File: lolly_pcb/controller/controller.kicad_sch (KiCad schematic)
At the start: 1 part, among them U1 ESP32-S2-MINI-1

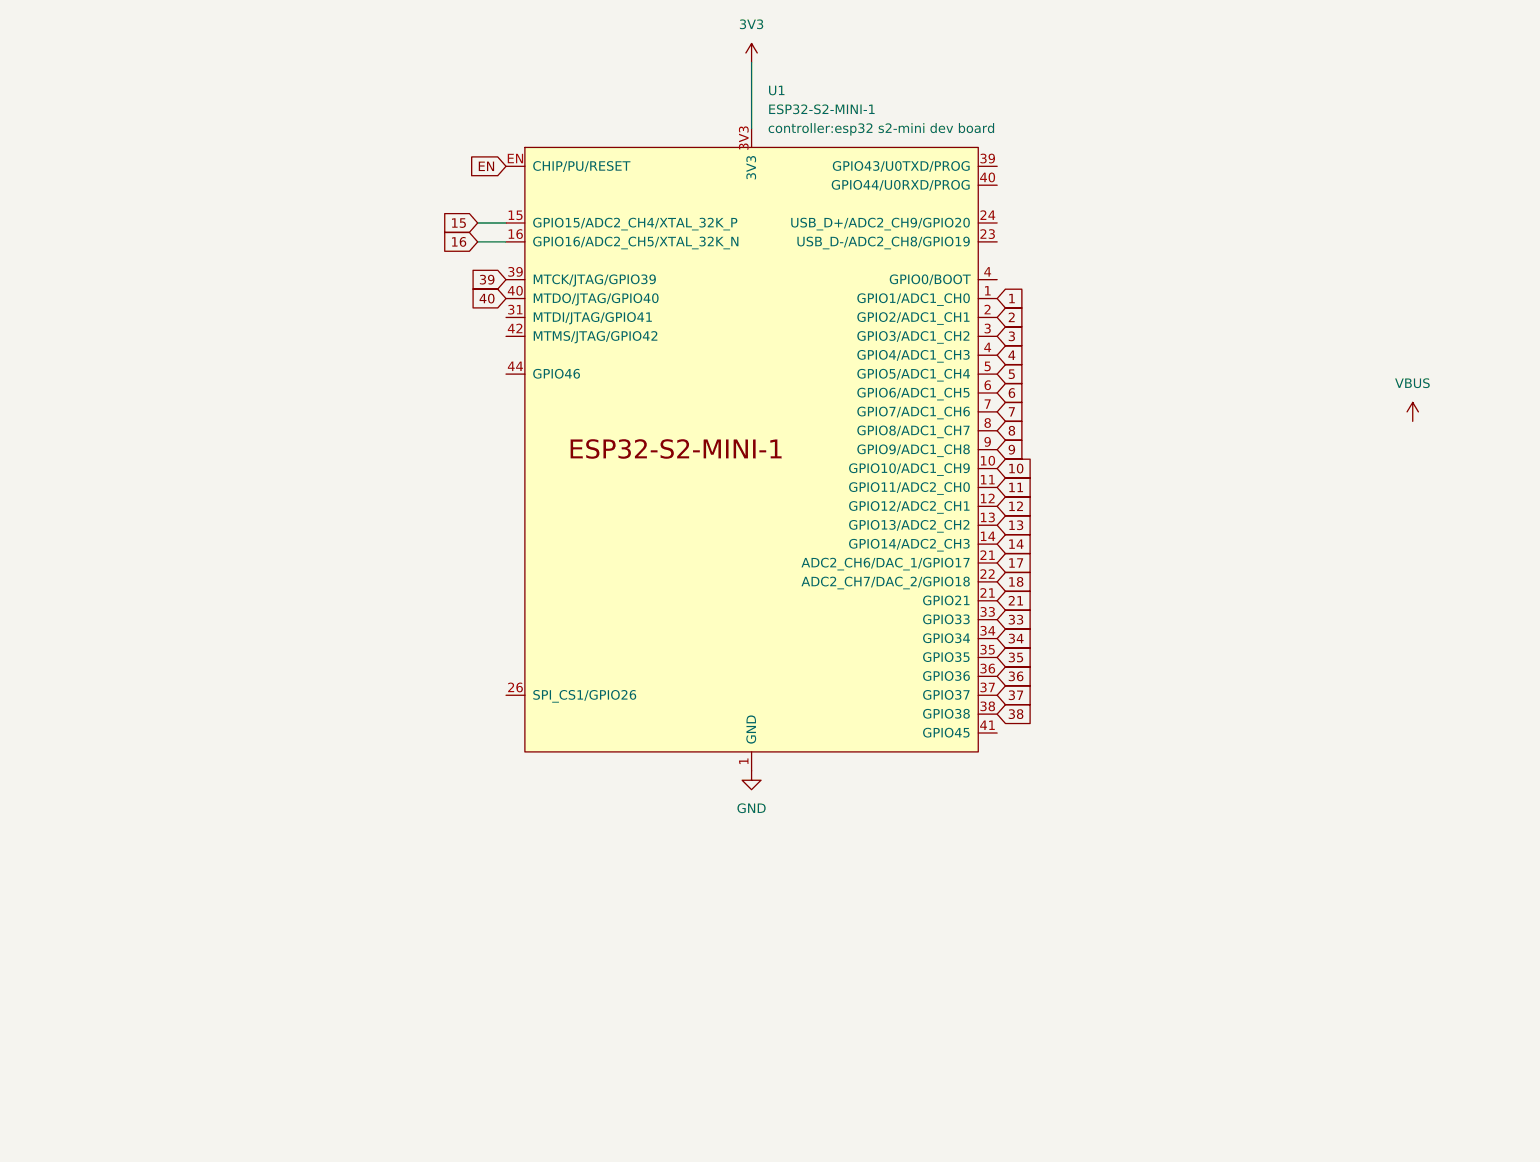
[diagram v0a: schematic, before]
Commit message: add charging circuit, connector and switch
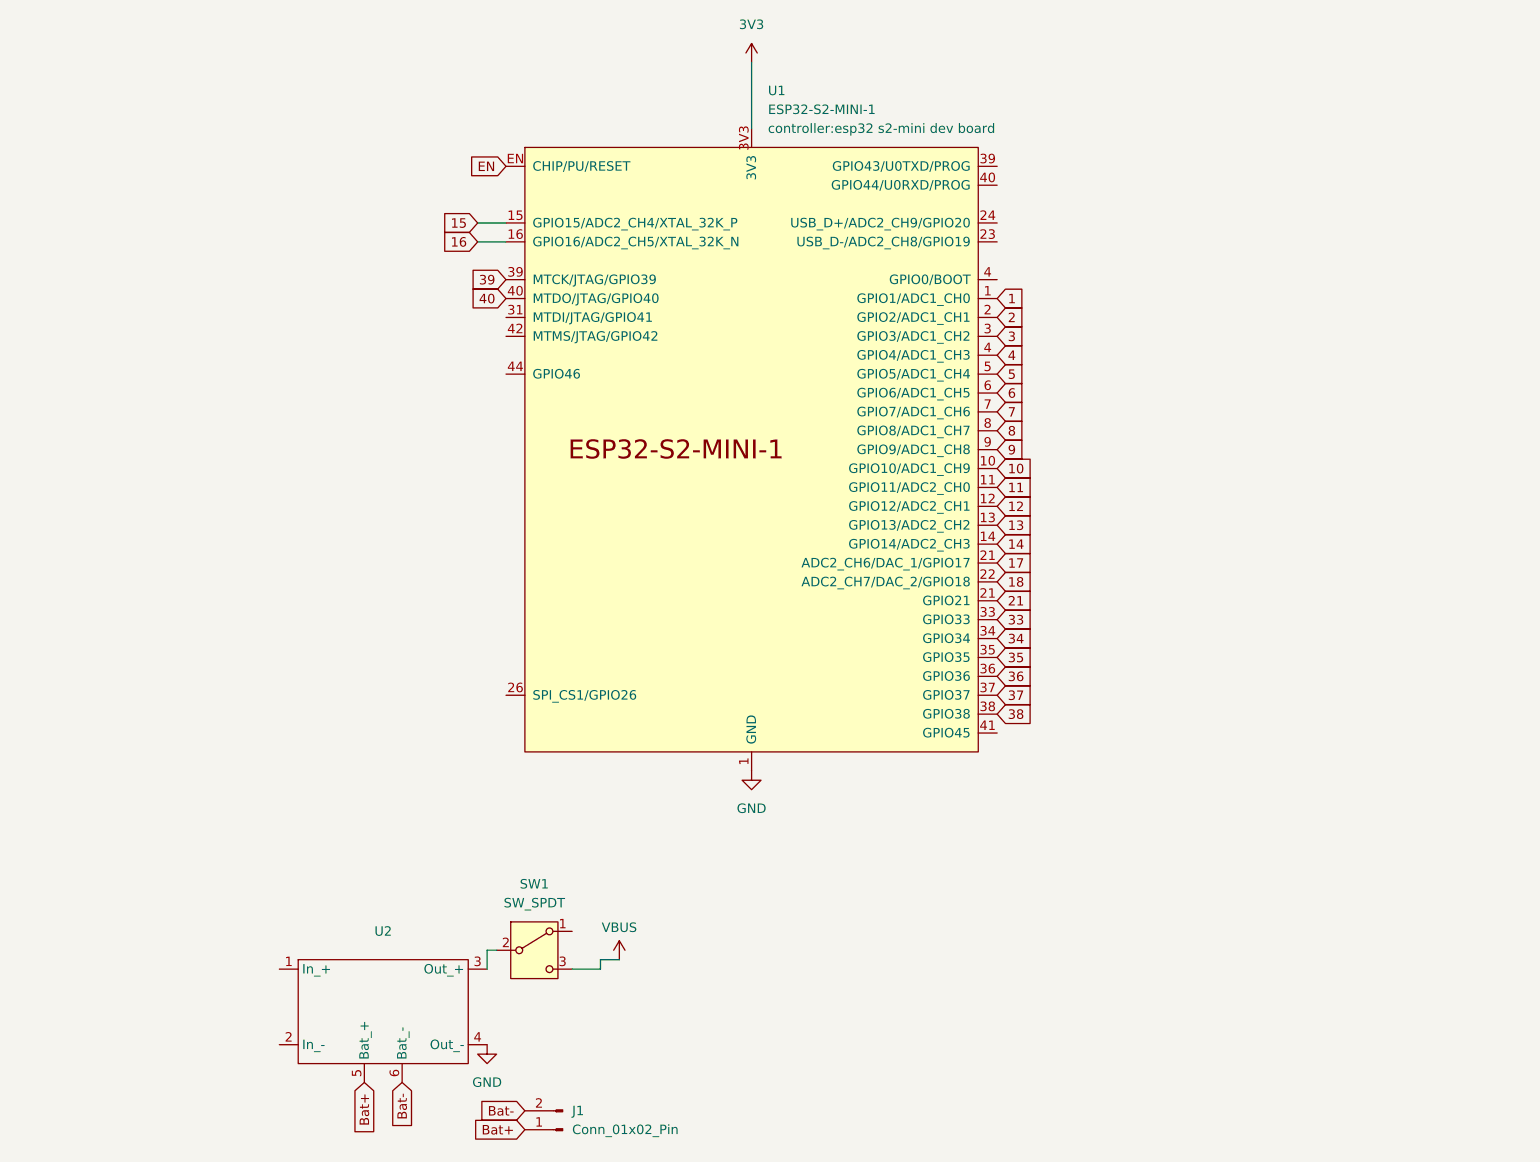
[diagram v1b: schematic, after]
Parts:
- added J1: Conn_01x02_Pin, Connector_JST:JST_PH_S2B-PH-K_1x02_P2.00mm_Horizontal, symbol Connector:Conn_01x02_Pin
- added SW1: SW_SPDT, controller:1P2T SPDT RUNCCI-YUN, symbol Switch:SW_SPDT
- added U2: ~, controller:tp4056 module, symbol lolly_comp:tp4056_module
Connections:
- net GND: now also U2.4 (Out_-)
- net VBUS: now also SW1.3 (C)
- new net: SW1.2 (B), U2.3 (Out_+)
- new net Bat+: J1.1 (Pin_1), U2.5 (Bat_+)
- new net Bat-: J1.2 (Pin_2), U2.6 (Bat_-)

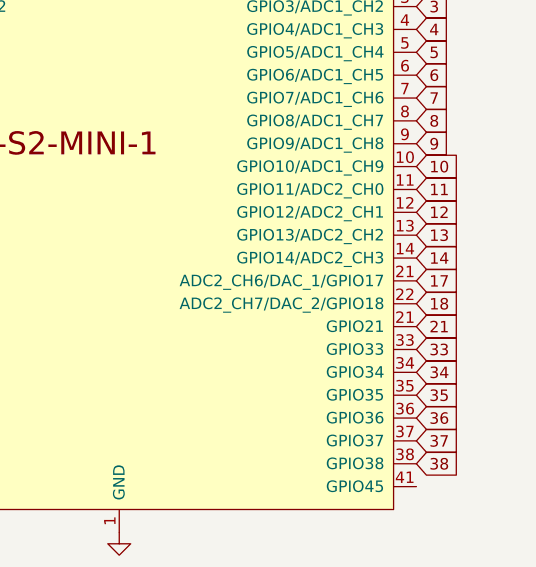
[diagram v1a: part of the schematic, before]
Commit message: first proper layout
includes solder pads for later components, better antenna placement, and routing
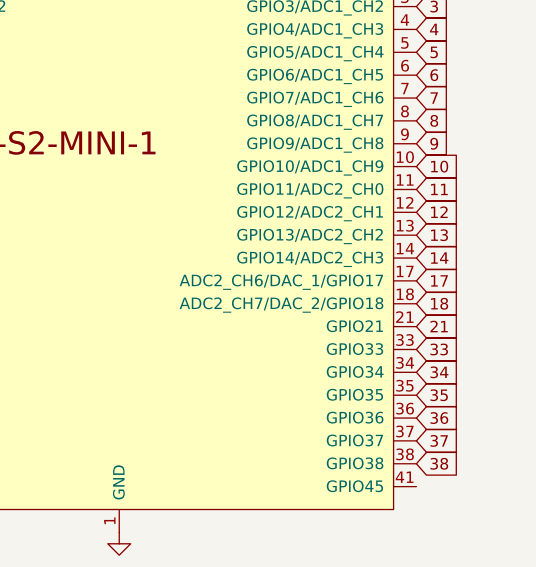
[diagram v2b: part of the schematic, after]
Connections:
- net 17: now also U1.17 (ADC2_CH6/DAC_1/GPIO17); no longer U1.21 (GPIO21)
- net 18: now also U1.18 (ADC2_CH7/DAC_2/GPIO18); no longer U1.22 (ADC2_CH7/DAC_2/GPIO18)
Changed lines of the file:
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@@
 		(pin "21"
 		)
-		(pin "21"
+		(pin "17"
 		)
-		(pin "22"
+		(pin "18"
 		)
 		(pin "23"

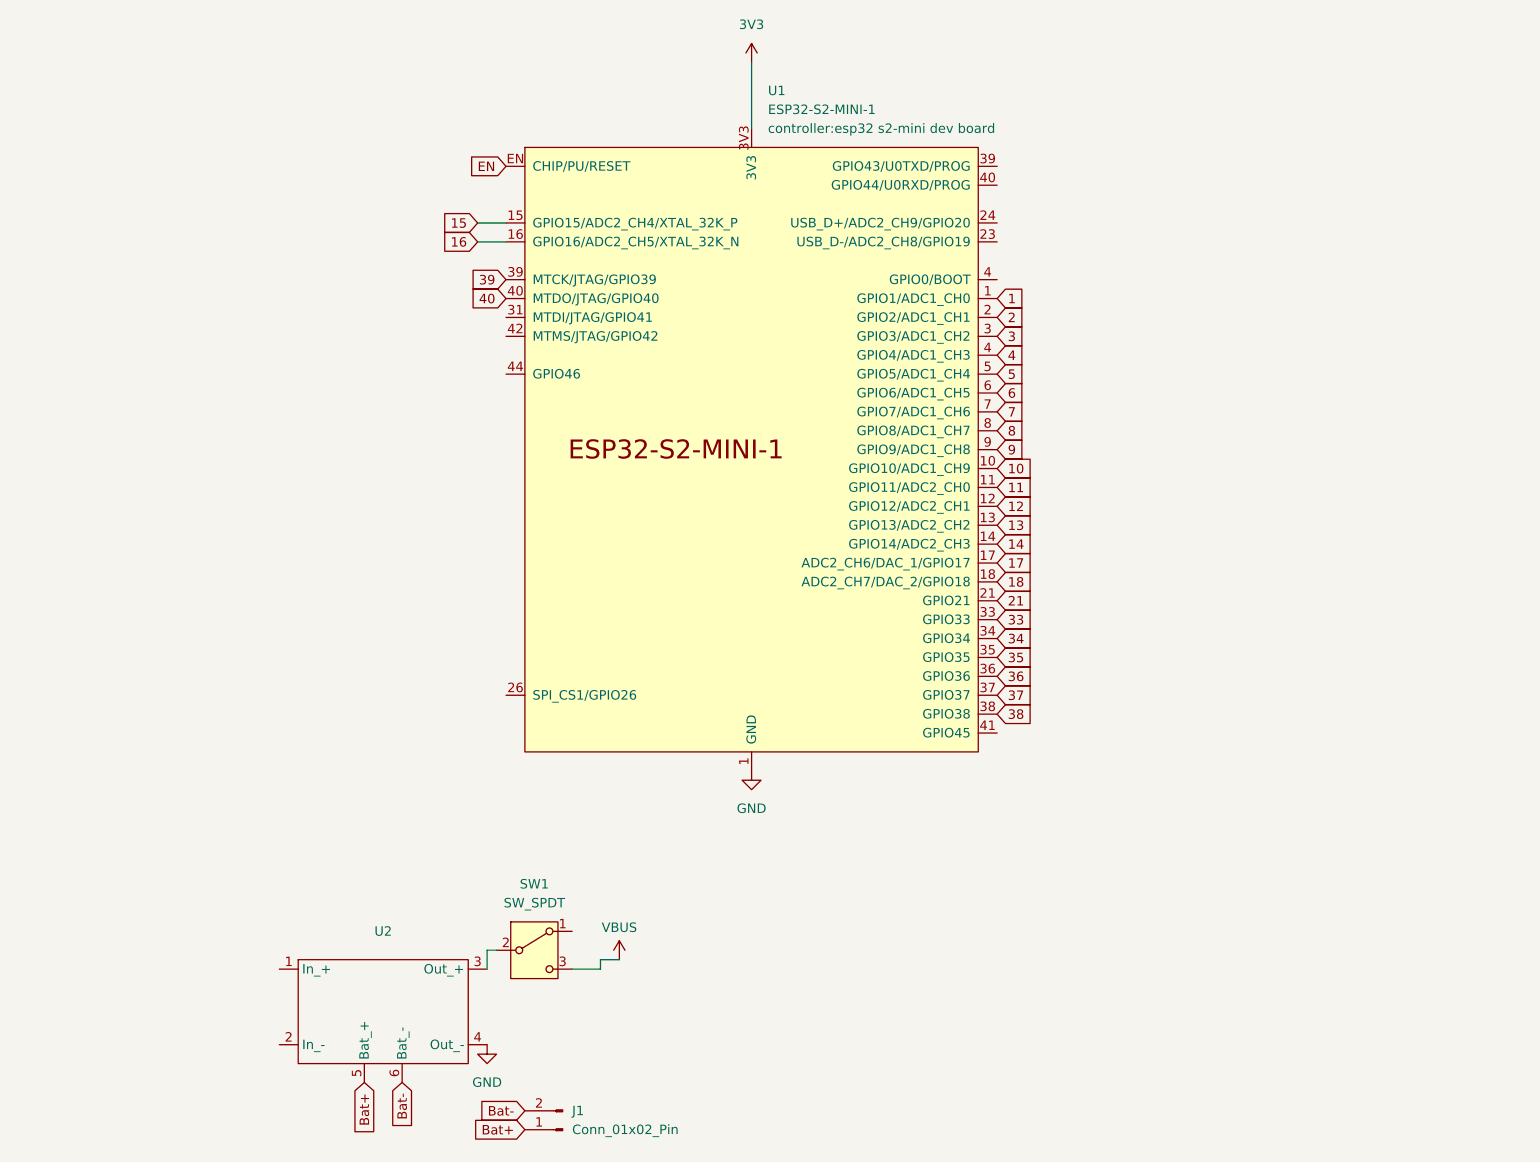
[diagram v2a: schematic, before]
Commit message: rearrange board for usb-c breakout board
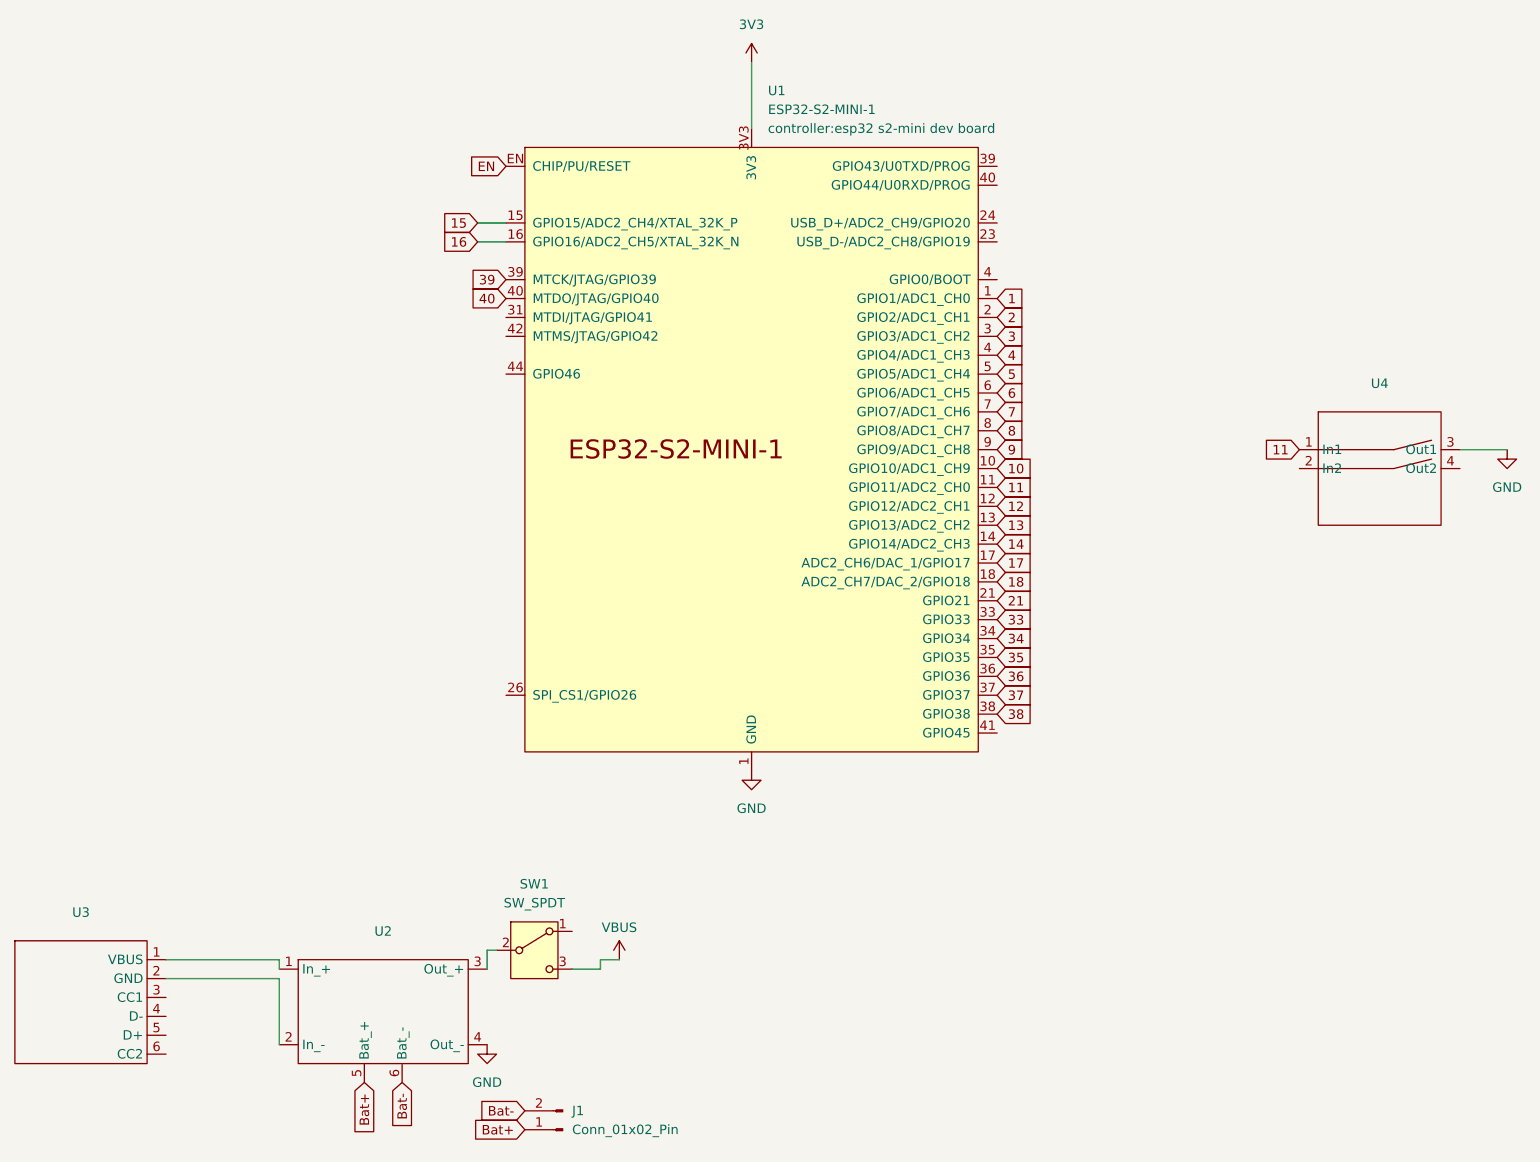
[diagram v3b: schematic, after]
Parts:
- added U3: ~, controller:usb-c 5v breakout, symbol lolly_comp:usb-c_5v_breakout
- added U4: ~, symbol lolly_comp:Small_through_hole_button
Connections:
- net 11: now also U4.1 (In1)
- net GND: now also U4.3 (Out1)
- net at U2.1 (In_+): now also U3.1 (VBUS)
- net at U2.2 (In_-): now also U3.2 (GND)

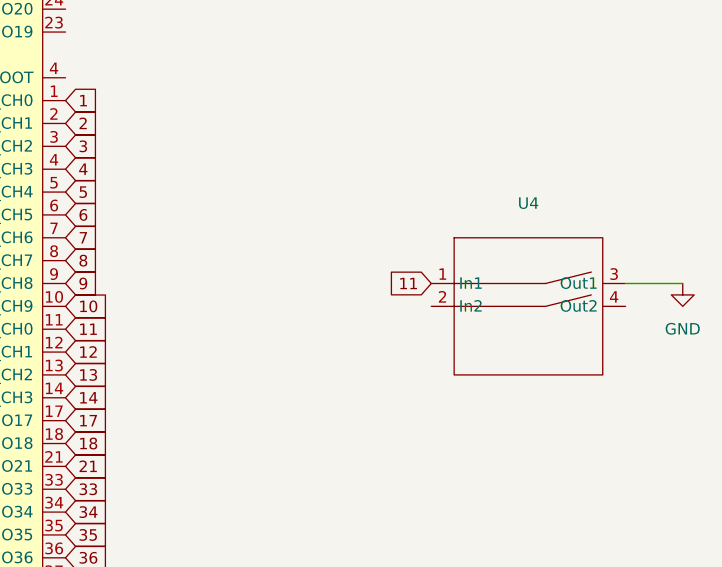
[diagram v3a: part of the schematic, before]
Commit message: use pin no. 5 for button
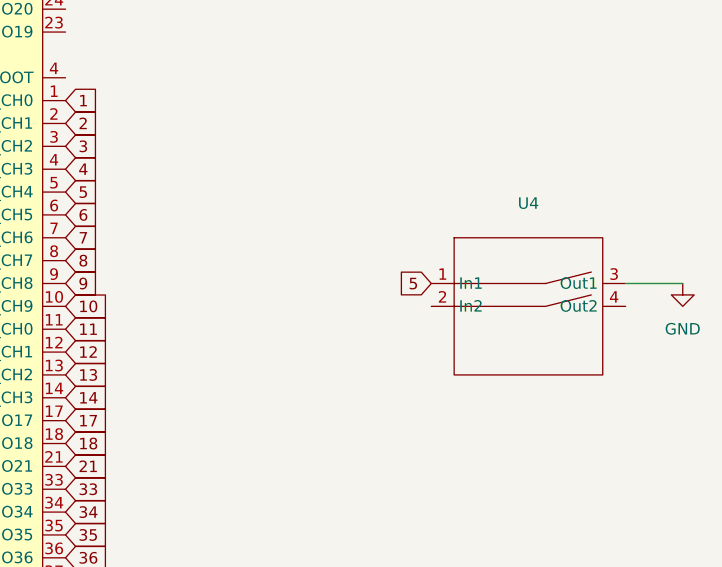
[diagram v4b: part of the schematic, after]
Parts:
- U4: footprint (none) -> controller:small thoughhole button
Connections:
- net 11: no longer U4.1 (In1)
- net 5: now also U4.1 (In1)
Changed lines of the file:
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@@
 		)
 	)
-	(global_label "11"
+	(global_label "5"
 		(shape input)
 		(at 203.2 85.09 180)
@@
 		)
 		(property "Intersheetrefs" "${INTERSHEET_REFS}"
-			(at 197.7958 85.09 0)
+			(at 199.0053 85.09 0)
 			(effects
 				(font
@@
 			)
 		)
-		(property "Footprint" ""
+		(property "Footprint" "controller:small thoughhole button"
 			(at 214.63 86.36 0)
 			(effects
